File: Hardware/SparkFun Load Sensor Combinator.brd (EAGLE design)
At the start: 27.9 x 30.5 mm, 14 parts

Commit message: Reverting Eagle files back to what is being sold on store front
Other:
- board text added: "B"
- board text added: "R"
- board text added: "W"
- board text added: "v10"
- board text removed: "+"
- board text removed: "-"
- board text removed: "C"
- board text removed: "v11"
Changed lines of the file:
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@@
 <layer number="127" name="_tValues" color="7" fill="1" visible="no" active="yes"/>
 <layer number="128" name="_bValues" color="7" fill="1" visible="no" active="yes"/>
-<layer number="129" name="Mask" color="7" fill="1" visible="no" active="yes"/>
+<layer number="129" name="Mask" color="7" fill="1" visible="yes" active="yes"/>
 <layer number="131" name="tAdjust" color="7" fill="1" visible="no" active="yes"/>
 <layer number="132" name="bAdjust" color="7" fill="1" visible="no" active="yes"/>
@@
 <layer number="223" name="223bmp" color="24" fill="1" visible="no" active="no"/>
 <layer number="224" name="224bmp" color="25" fill="1" visible="no" active="no"/>
-<layer number="225" name="225bmp" color="7" fill="1" visible="no" active="yes"/>
-<layer number="226" name="226bmp" color="7" fill="1" visible="no" active="yes"/>
-<layer number="227" name="227bmp" color="7" fill="1" visible="no" active="yes"/>
-<layer number="228" name="228bmp" color="7" fill="1" visible="no" active="yes"/>
-<layer number="229" name="229bmp" color="7" fill="1" visible="no" active="yes"/>
-<layer number="230" name="230bmp" color="7" fill="1" visible="no" active="yes"/>
-<layer number="231" name="231bmp" color="7" fill="1" visible="no" active="yes"/>
+<layer number="225" name="225bmp" color="7" fill="1" visible="yes" active="yes"/>
+<layer number="226" name="226bmp" color="7" fill="1" visible="yes" active="yes"/>
+<layer number="227" name="227bmp" color="7" fill="1" visible="yes" active="yes"/>
+<layer number="228" name="228bmp" color="7" fill="1" visible="yes" active="yes"/>
+<layer number="229" name="229bmp" color="7" fill="1" visible="yes" active="yes"/>
+<layer number="230" name="230bmp" color="7" fill="1" visible="yes" active="yes"/>
+<layer number="231" name="231bmp" color="7" fill="1" visible="yes" active="yes"/>
 <layer number="248" name="Housing" color="7" fill="1" visible="no" active="yes"/>
 <layer number="249" name="Edge" color="7" fill="1" visible="no" active="yes"/>
@@
 <layer number="251" name="SMDround" color="12" fill="11" visible="no" active="no"/>
 <layer number="254" name="cooling" color="7" fill="1" visible="no" active="yes"/>
-<layer number="255" name="routoute" color="7" fill="1" visible="no" active="yes"/>
+<layer number="255" name="routoute" color="7" fill="1" visible="yes" active="yes"/>
 </layers>
 <board>
@@
 <text x="13.335" y="6.477" size="1.27" layer="21" font="vector" ratio="15" rot="R270">WHT</text>
 <text x="18.415" y="6.477" size="1.27" layer="21" font="vector" ratio="15" rot="R270">RED</text>
+<text x="10.795" y="2.794" size="1.27" layer="22" font="vector" ratio="15" rot="MR90">A+</text>
 <text x="13.335" y="2.794" size="1.27" layer="22" font="vector" ratio="15" rot="MR90">A-</text>
-<text x="10.795" y="2.794" size="1.27" layer="22" font="vector" ratio="15" rot="MR90">A+</text>
 <text x="15.875" y="2.794" size="1.27" layer="22" font="vector" ratio="15" rot="MR90">E-</text>
 <text x="18.415" y="2.794" size="1.27" layer="22" font="vector" ratio="15" rot="MR90">E+</text>
-<text x="5.334" y="15.748" size="1.27" layer="21" font="vector" ratio="15">UL</text>
+<text x="20.574" y="15.748" size="1.27" layer="21" font="vector" ratio="15">UL</text>
 <text x="15.494" y="15.748" size="1.27" layer="21" font="vector" ratio="15">UR</text>
 <text x="10.414" y="15.748" size="1.27" layer="21" font="vector" ratio="15">LL</text>
-<text x="20.574" y="15.748" size="1.27" layer="21" font="vector" ratio="15">LR</text>
+<text x="5.334" y="15.748" size="1.27" layer="21" font="vector" ratio="15">LR</text>
 <text x="23.876" y="13.97" size="1.27" layer="21" font="vector" ratio="15" rot="R270">Load</text>
 <text x="15.24" y="7.366" size="1.27" layer="22" font="vector" ratio="15" rot="MR180">UR</text>
 <text x="10.16" y="7.366" size="1.27" layer="22" font="vector" ratio="15" rot="MR180">LL</text>
-<text x="20.32" y="7.366" size="1.27" layer="22" font="vector" ratio="15" rot="MR180">LR</text>
-<text x="5.08" y="7.366" size="1.27" layer="22" font="vector" ratio="15" rot="MR180">UL</text>
+<text x="5.08" y="7.366" size="1.27" layer="22" font="vector" ratio="15" rot="MR180">LR</text>
+<text x="20.32" y="7.366" size="1.27" layer="22" font="vector" ratio="15" rot="MR180">UL</text>
 <text x="25.654" y="15.621" size="1.27" layer="21" font="vector" ratio="15" rot="R270">Sensors</text>
-<text x="9.906" y="14.859" size="1.778" layer="21" font="vector" ratio="15" rot="R180">-</text>
-<text x="9.906" y="12.319" size="1.778" layer="21" font="vector" ratio="15" rot="R180">+</text>
-<text x="9.906" y="9.779" size="1.778" layer="21" font="vector" ratio="15" rot="R180">C</text>
-<text x="14.986" y="14.859" size="1.778" layer="21" font="vector" ratio="15" rot="R180">-</text>
-<text x="14.986" y="12.319" size="1.778" layer="21" font="vector" ratio="15" rot="R180">+</text>
-<text x="20.066" y="9.779" size="1.778" layer="21" font="vector" ratio="15" rot="R180">C</text>
-<text x="20.066" y="14.859" size="1.778" layer="21" font="vector" ratio="15" rot="R180">-</text>
-<text x="20.066" y="12.319" size="1.778" layer="21" font="vector" ratio="15" rot="R180">+</text>
-<text x="14.986" y="9.779" size="1.778" layer="21" font="vector" ratio="15" rot="R180">C</text>
-<text x="0.762" y="4.953" size="1.778" layer="16" font="vector" ratio="15" rot="MR90">v11</text>
+<text x="9.906" y="14.859" size="1.778" layer="21" font="vector" ratio="15" rot="R180">B</text>
+<text x="9.906" y="12.319" size="1.778" layer="21" font="vector" ratio="15" rot="R180">W</text>
+<text x="9.906" y="9.779" size="1.778" layer="21" font="vector" ratio="15" rot="R180">R</text>
+<text x="14.986" y="14.859" size="1.778" layer="21" font="vector" ratio="15" rot="R180">B</text>
+<text x="14.986" y="12.319" size="1.778" layer="21" font="vector" ratio="15" rot="R180">W</text>
+<text x="14.986" y="9.779" size="1.778" layer="21" font="vector" ratio="15" rot="R180">R</text>
+<text x="20.066" y="14.859" size="1.778" layer="21" font="vector" ratio="15" rot="R180">B</text>
+<text x="20.066" y="12.319" size="1.778" layer="21" font="vector" ratio="15" rot="R180">W</text>
+<text x="20.066" y="9.779" size="1.778" layer="21" font="vector" ratio="15" rot="R180">R</text>
+<text x="0.762" y="4.953" size="1.778" layer="16" font="vector" ratio="15" rot="MR90">v10</text>
 <text x="8.255" y="6.477" size="1.27" layer="21" font="vector" ratio="15" rot="R270">YLW</text>
 <text x="8.255" y="2.794" size="1.27" layer="22" font="vector" ratio="15" rot="MR90">SLD</text>
@@
 <signal name="A+">
 <contactref element="JP3" pad="3"/>
+<wire x1="11.43" y1="8.89" x2="11.43" y2="1.27" width="0.508" layer="1"/>
 <contactref element="JP6" pad="5"/>
 <wire x1="11.43" y1="8.89" x2="10.16" y2="8.89" width="0.508" layer="1"/>
@@
 <wire x1="13.335" y1="23.495" x2="12.7" y2="24.13" width="0.508" layer="1"/>
 <contactref element="JP5" pad="4"/>
-<wire x1="11.43" y1="8.89" x2="11.43" y2="1.27" width="0.508" layer="1"/>
 </signal>
 <signal name="A-">
@@
 <wire x1="19.05" y1="14.605" x2="19.05" y2="10.16" width="0.508" layer="16"/>
 <contactref element="JP5" pad="3"/>
-<wire x1="16.51" y1="8.89" x2="13.97" y2="6.35" width="0.508" layer="1"/>
-<wire x1="13.97" y1="6.35" x2="13.97" y2="1.27" width="0.508" layer="1"/>
+<wire x1="13.97" y1="1.27" x2="13.97" y2="6.35" width="0.508" layer="1"/>
+<wire x1="13.97" y1="6.35" x2="16.51" y2="8.89" width="0.508" layer="1"/>
 </signal>
 <signal name="E-">

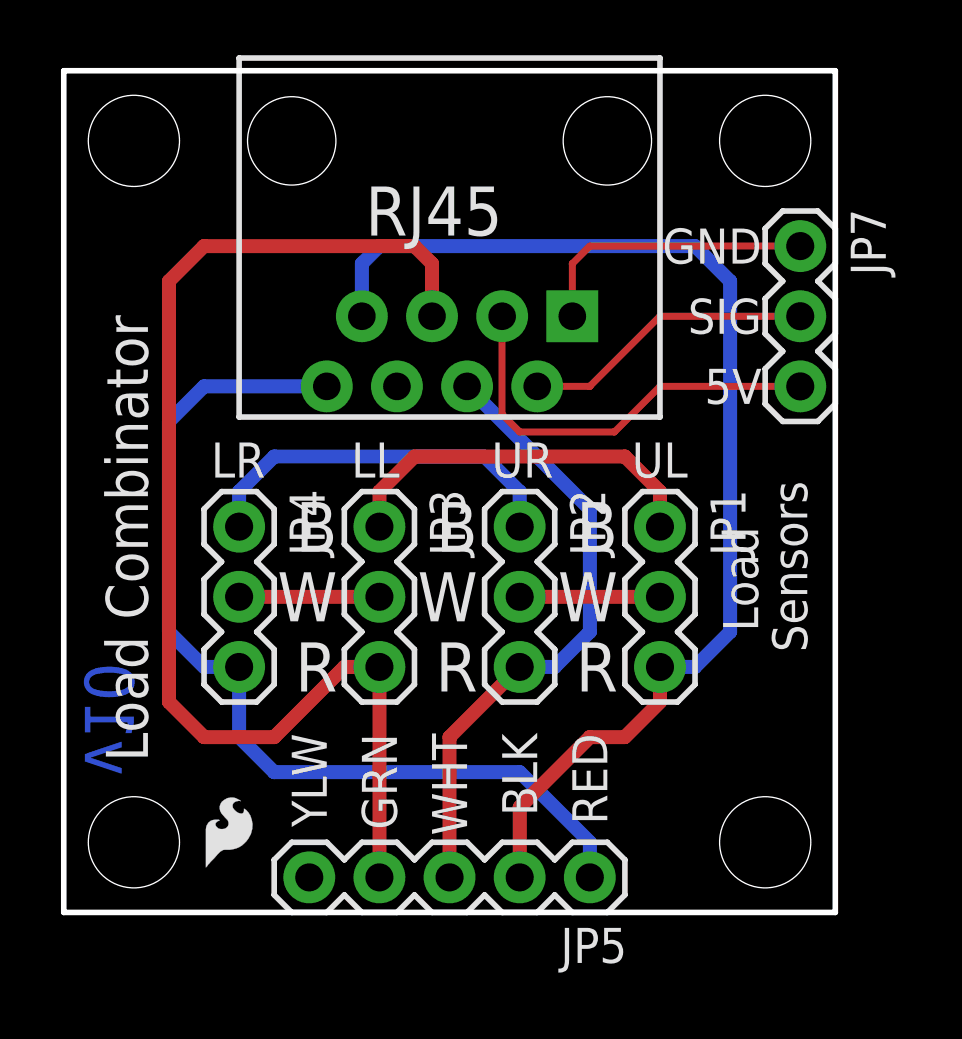
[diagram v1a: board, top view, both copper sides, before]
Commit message: Revision 11 changes
Updated labels from R/W/B to +/-/C and moved temp sensor pins down away
from standoff.
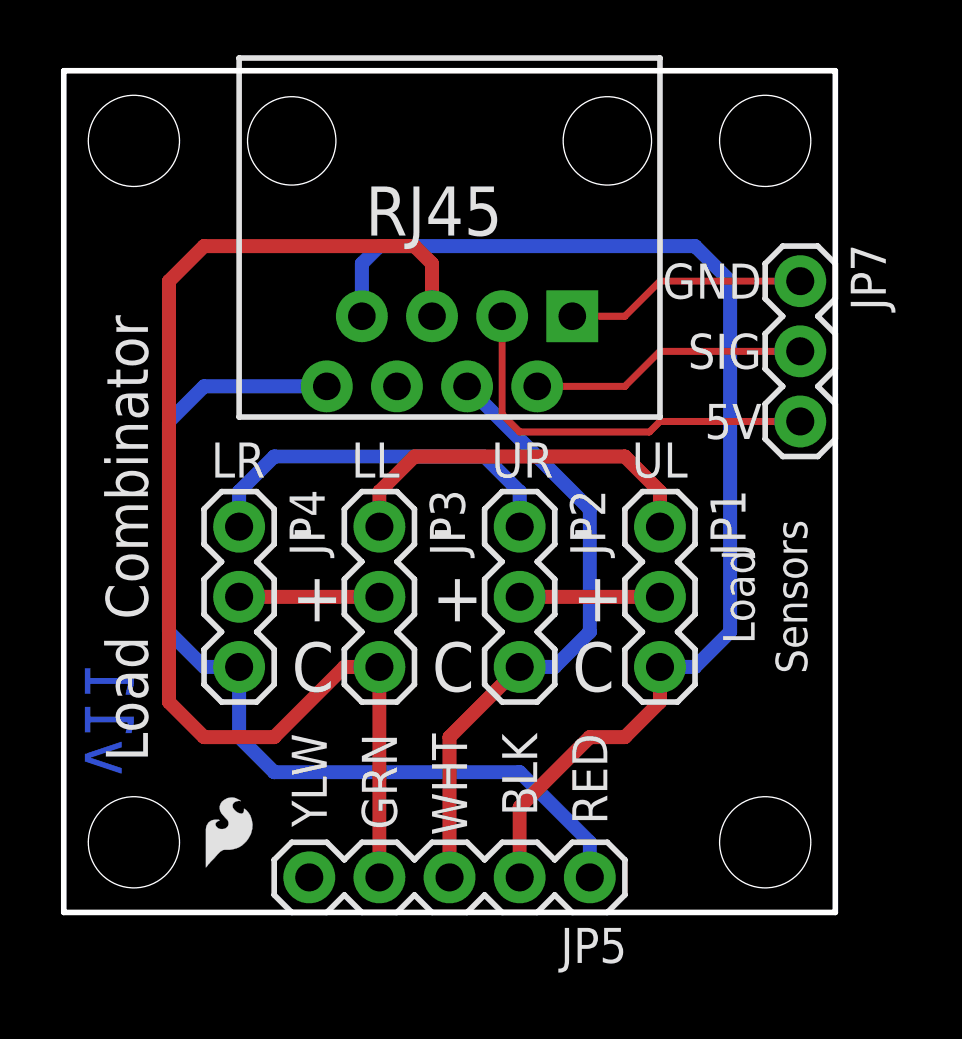
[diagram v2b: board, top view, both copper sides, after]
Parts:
- moved JP7 1.27 mm to (26.7, 22.9)
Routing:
- net GND: track 10.4 -> 8.78 mm
- net TEMP_DAT: track 10.6 -> 10.1 mm
- net 5V: track 15.3 -> 14.8 mm
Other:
- board text added: "+"
- board text added: "-"
- board text added: "A. Wende"
- board text added: "C"
- board text added: "Revised by:"
- board text added: "v11"
- board text removed: "B"
- board text removed: "R"
- board text removed: "W"
- board text removed: "v10"
